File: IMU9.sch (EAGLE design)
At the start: 22 parts, among them IC1 MCP1700T-3302E/TT, Q1 RJU003N03 N-MOSFET, Q2 RJU003N03 N-MOSFET

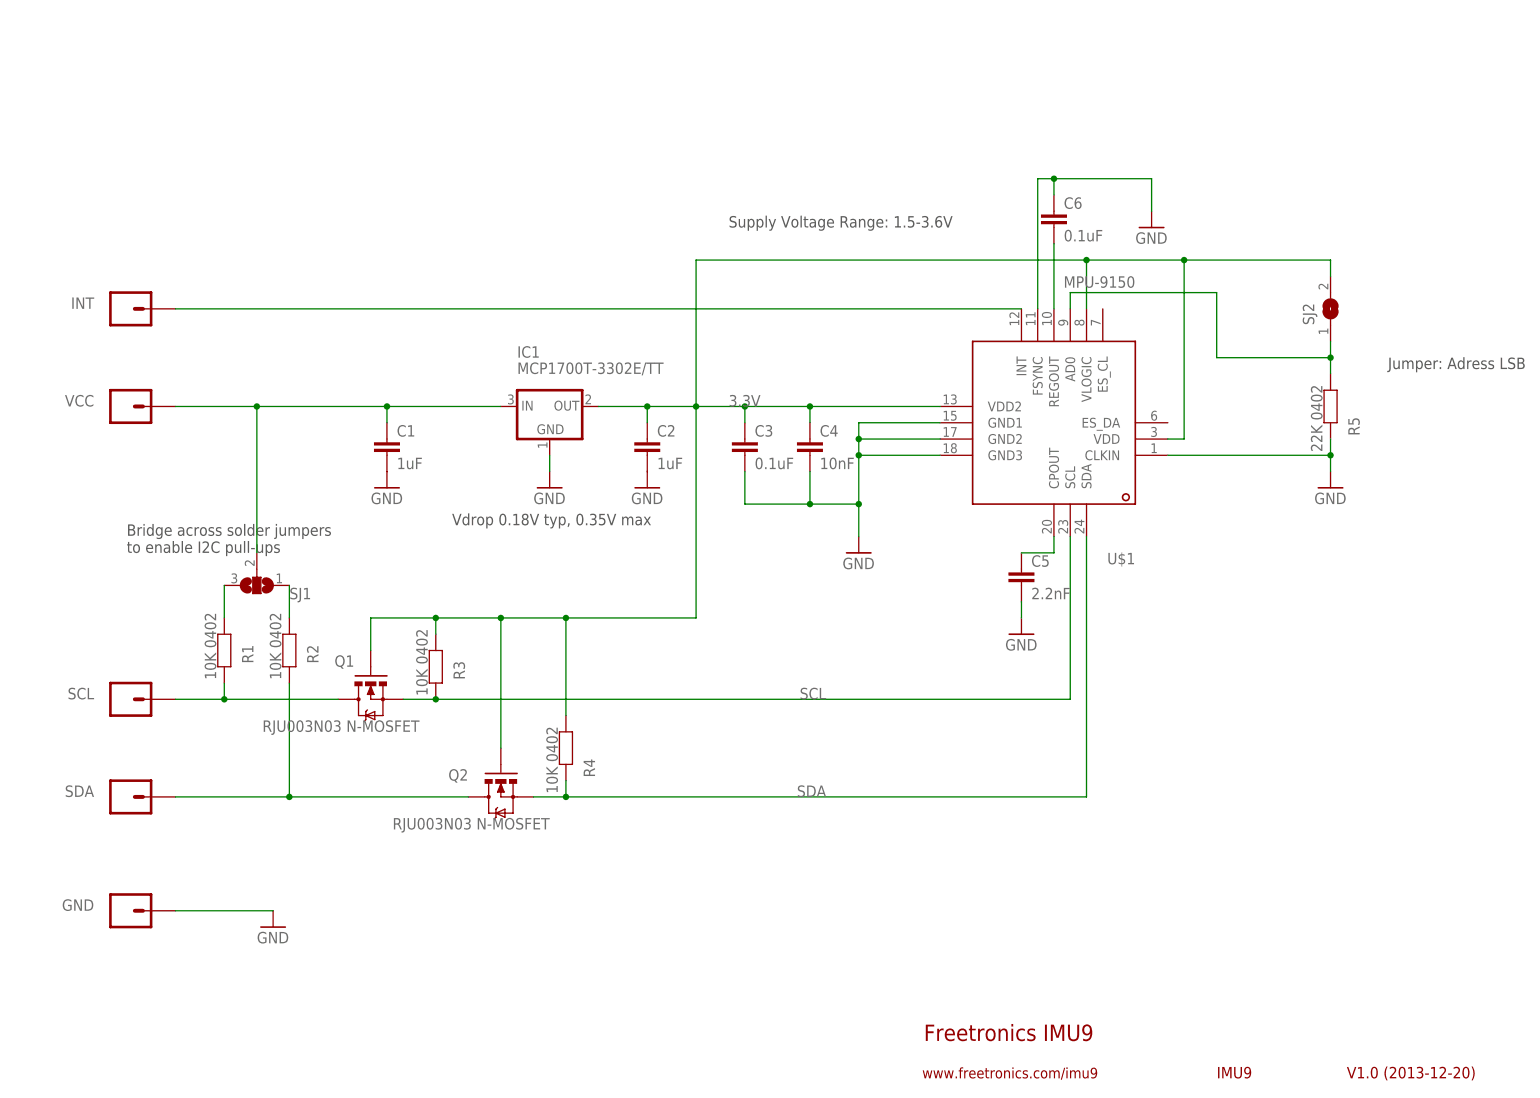
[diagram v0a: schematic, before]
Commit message: Added Adelmo Eloy as designer Added notes to schematic about max parameters Improved silkscreen Improved designator positions Improved part designators and values
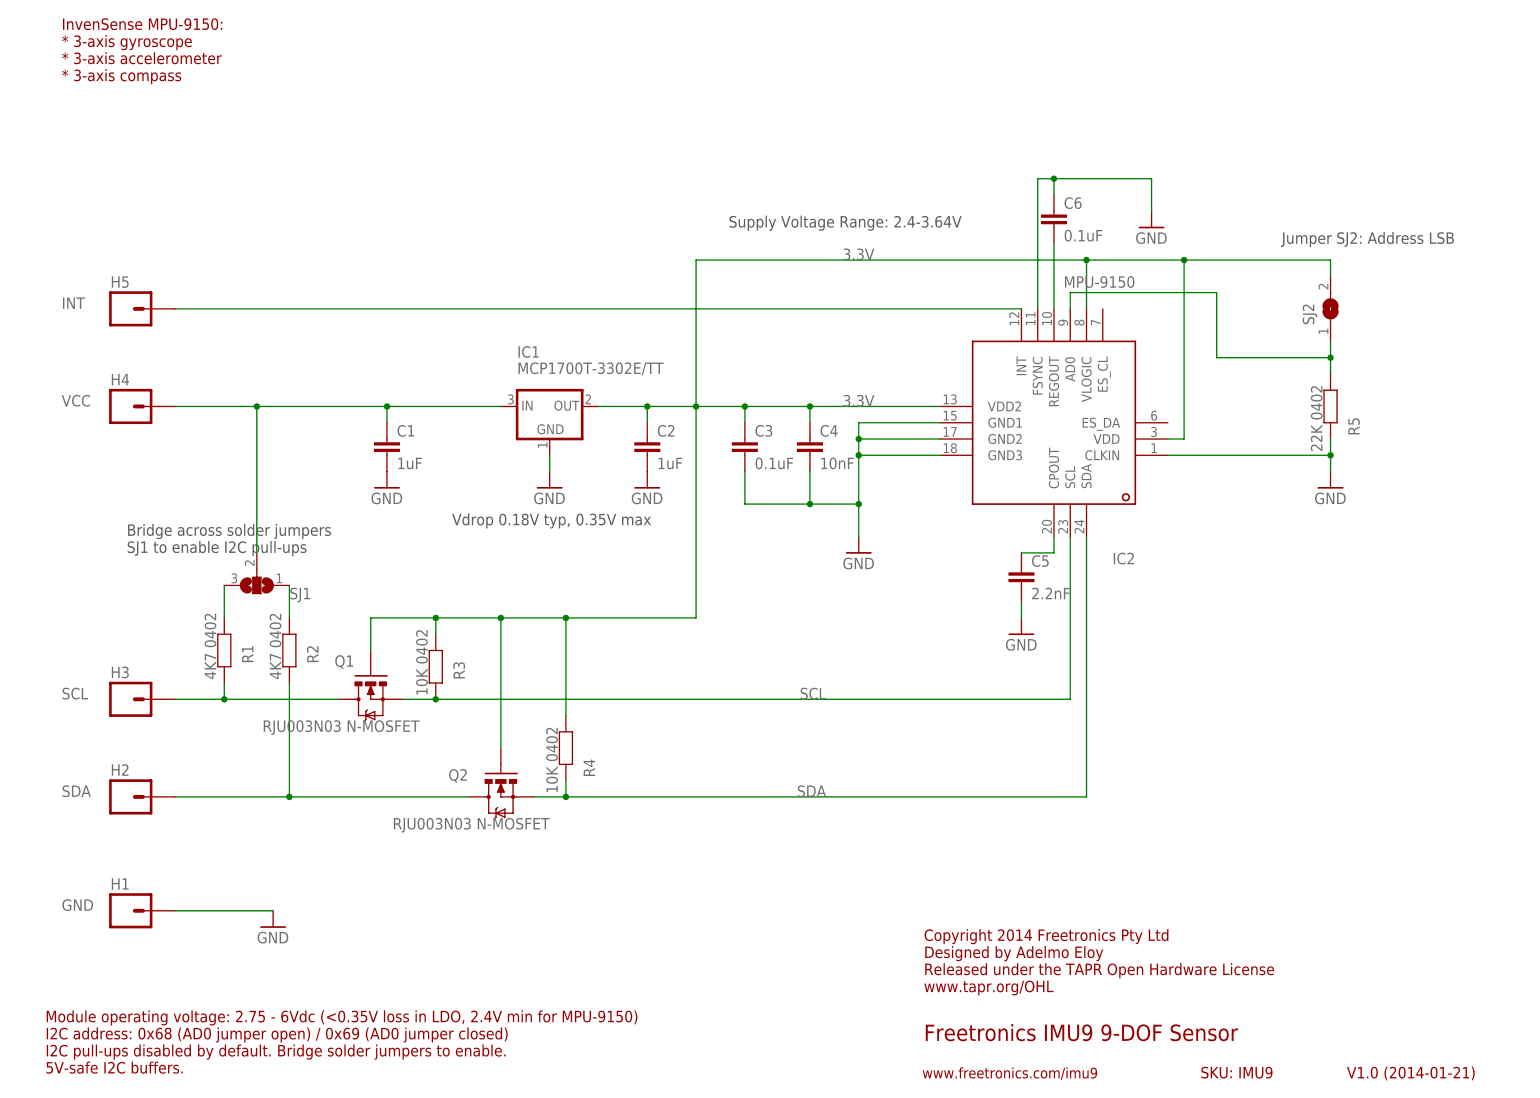
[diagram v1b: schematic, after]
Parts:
- H1: value M01PTH -> GND
- H2: value M01PTH -> SDA
- H3: value M01PTH -> SCL
- H4: value M01PTH -> VCC
- H5: value M01PTH -> INT
- R1, R2: value 10K 0402 -> 4K7 0402
- renumbered GND to H1, INT to H5, SCL to H3, SDA to H2, U$1 to IC2, VCC to H4
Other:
- note added: "Bridge across solder jumpers SJ1 to enable I2C pull-ups"
- note added: "Copyright 2014 Freetronics Pty Ltd Designed by Adelmo Eloy Released under the TAPR Open Hardware License www.tapr.org/OHL"
- note added: "Freetronics IMU9 9-DOF Sensor"
- note added: "InvenSense MPU-9150: * 3-axis gyroscope * 3-axis accelerometer * 3-axis compass"
- note added: "Jumper SJ2: Address LSB"
- note added: "Module operating voltage: 2.75 - 6Vdc (<0.35V loss in LDO, 2.4V min for MPU-9150) I2C address: 0x68 (AD0 jumper open) / 0x69 (AD0 jumper closed) I2C pull-ups disabled by default. Bridge solder jumpers to enable. 5V-safe I2C buffers."
- note added: "SKU: IMU9"
- note added: "Supply Voltage Range: 2.4-3.64V"
- note added: "V1.0 (2014-01-21)"
- note removed: "Bridge across solder jumpers to enable I2C pull-ups"
- note removed: "Freetronics IMU9"
- note removed: "IMU9"
- note removed: "Jumper: Adress LSB"
- note removed: "Supply Voltage Range: 1.5-3.6V"
- note removed: "V1.0 (2013-12-20)"

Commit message: Bridged across I2C pull-up cut track jumpers Shortened URL
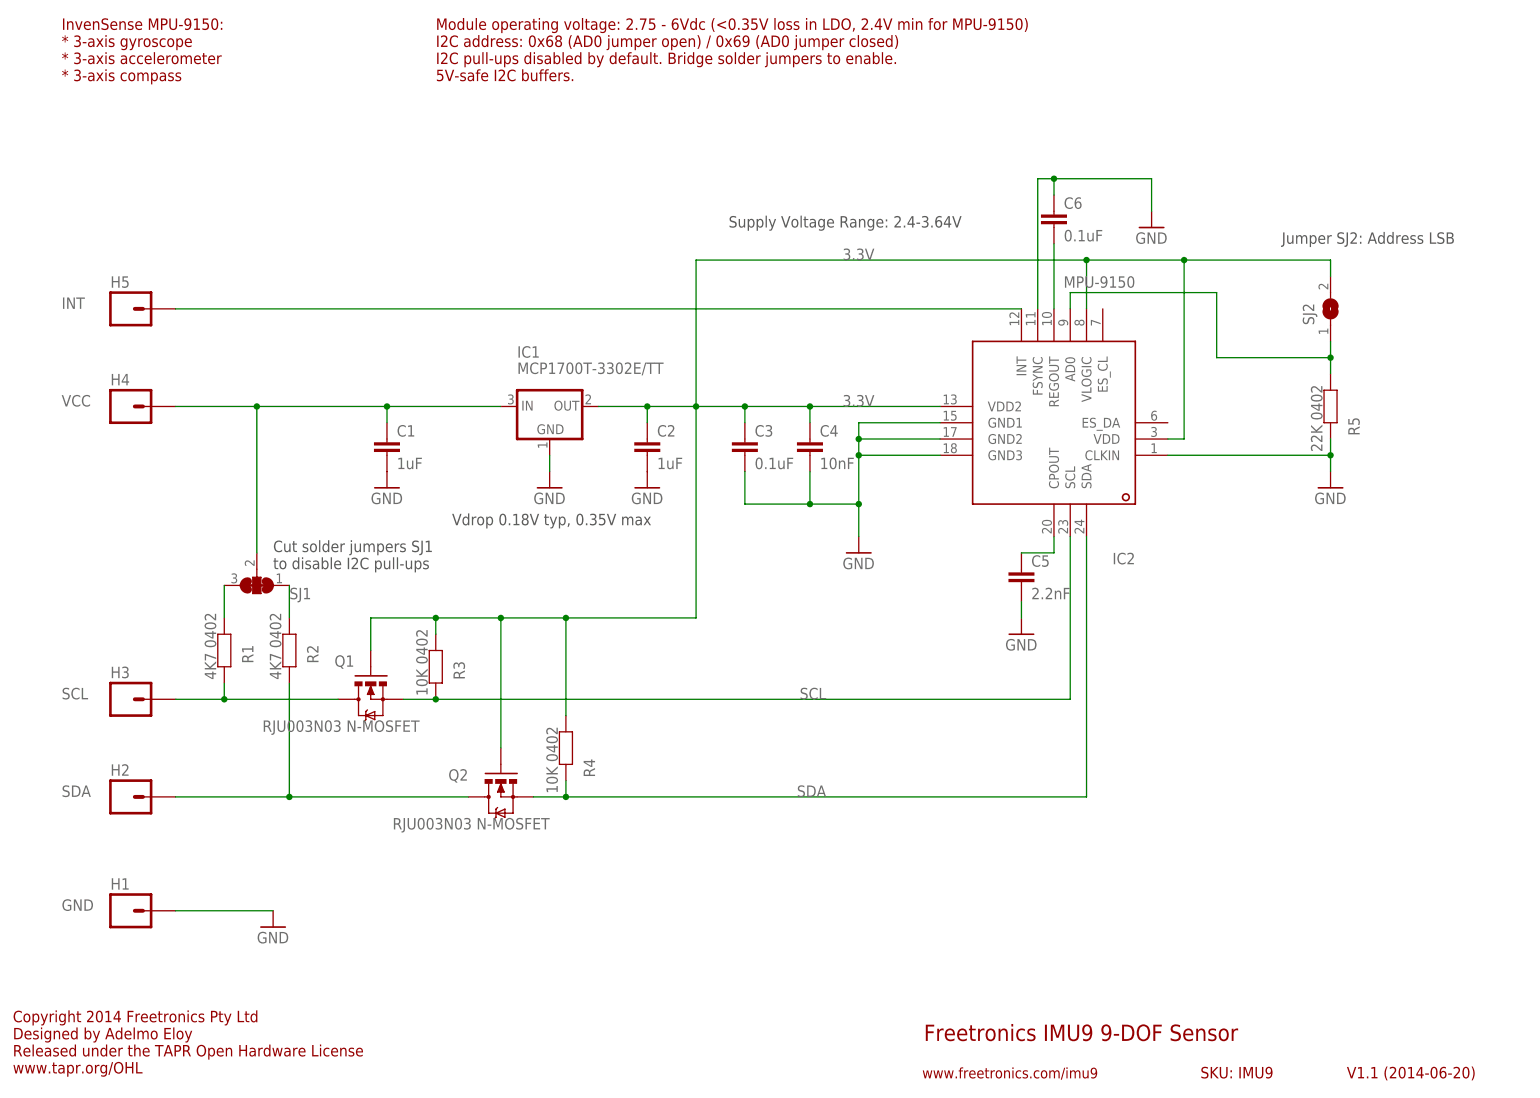
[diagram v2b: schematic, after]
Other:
- note added: "Cut solder jumpers SJ1 to disable I2C pull-ups"
- note added: "V1.1 (2014-06-20)"
- note removed: "Bridge across solder jumpers SJ1 to enable I2C pull-ups"
- note removed: "V1.0 (2014-01-21)"
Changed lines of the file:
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@@
 <?xml version="1.0" encoding="utf-8"?>
 <!DOCTYPE eagle SYSTEM "eagle.dtd">
-<eagle version="6.3">
+<eagle version="6.5.0">
 <drawing>
 <settings>
@@
 <plain>
 <text x="149.86" y="12.7" size="2.54" layer="94">Freetronics IMU9 9-DOF Sensor</text>
-<text x="215.9" y="6.858" size="1.778" layer="94">V1.0 (2014-01-21)</text>
+<text x="215.9" y="6.858" size="1.778" layer="94">V1.1 (2014-06-20)</text>
 <text x="149.606" y="6.858" size="1.651" layer="94">www.freetronics.com/imu9</text>
 <text x="193.04" y="6.858" size="1.778" layer="94">SKU: IMU9</text>
@@
 <frame x1="190.5" y1="5.08" x2="213.36" y2="10.16" columns="8" rows="5" layer="94"/>
 <frame x1="213.36" y1="5.08" x2="243.84" y2="10.16" columns="8" rows="5" layer="94"/>
-<text x="25.4" y="88.9" size="1.778" layer="97">Bridge across solder jumpers
-SJ1 to enable I2C pull-ups</text>
+<text x="48.26" y="86.36" size="1.778" layer="97">Cut solder jumpers SJ1
+to disable I2C pull-ups</text>
 <text x="76.2" y="93.218" size="1.778" layer="97">Vdrop 0.18V typ, 0.35V max</text>
 <text x="205.74" y="137.16" size="1.778" layer="97">Jumper SJ2: Address LSB</text>
-<text x="149.86" y="20.32" size="1.778" layer="94">Copyright 2014 Freetronics Pty Ltd
+<text x="7.62" y="7.62" size="1.778" layer="94">Copyright 2014 Freetronics Pty Ltd
 Designed by Adelmo Eloy
 Released under the TAPR Open Hardware License
@@
 * 3-axis accelerometer
 * 3-axis compass</text>
-<text x="12.7" y="7.62" size="1.778" layer="94">Module operating voltage: 2.75 - 6Vdc (&lt;0.35V loss in LDO, 2.4V min for MPU-9150)
+<text x="73.66" y="162.56" size="1.778" layer="94">Module operating voltage: 2.75 - 6Vdc (&lt;0.35V loss in LDO, 2.4V min for MPU-9150)
 I2C address: 0x68 (AD0 jumper open) / 0x69 (AD0 jumper closed)
 I2C pull-ups disabled by default. Bridge solder jumpers to enable.
 5V-safe I2C buffers.</text>
+<wire x1="43.18" y1="83.82" x2="48.26" y2="83.82" width="0.4064" layer="94"/>
 </plain>
 <instances>
